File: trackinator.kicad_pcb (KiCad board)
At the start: 4 copper layers, 83 x 33.1 mm, 97 parts, among them J1 Conn_01x04_Pin, SW1 TS-1187A-B-A-B, SW2 TS-1187A-B-A-B, U1 M24C02-WMN, U2 ESP32-S3FH4R2, U3 LMZ21701SILR, U4 LMZ21701SILR, U5 SP3481EN, U6 FE2.1, U7 SP3481EN, U8 SP3481EN, Y1 12Mhz, Y2 40Mhz

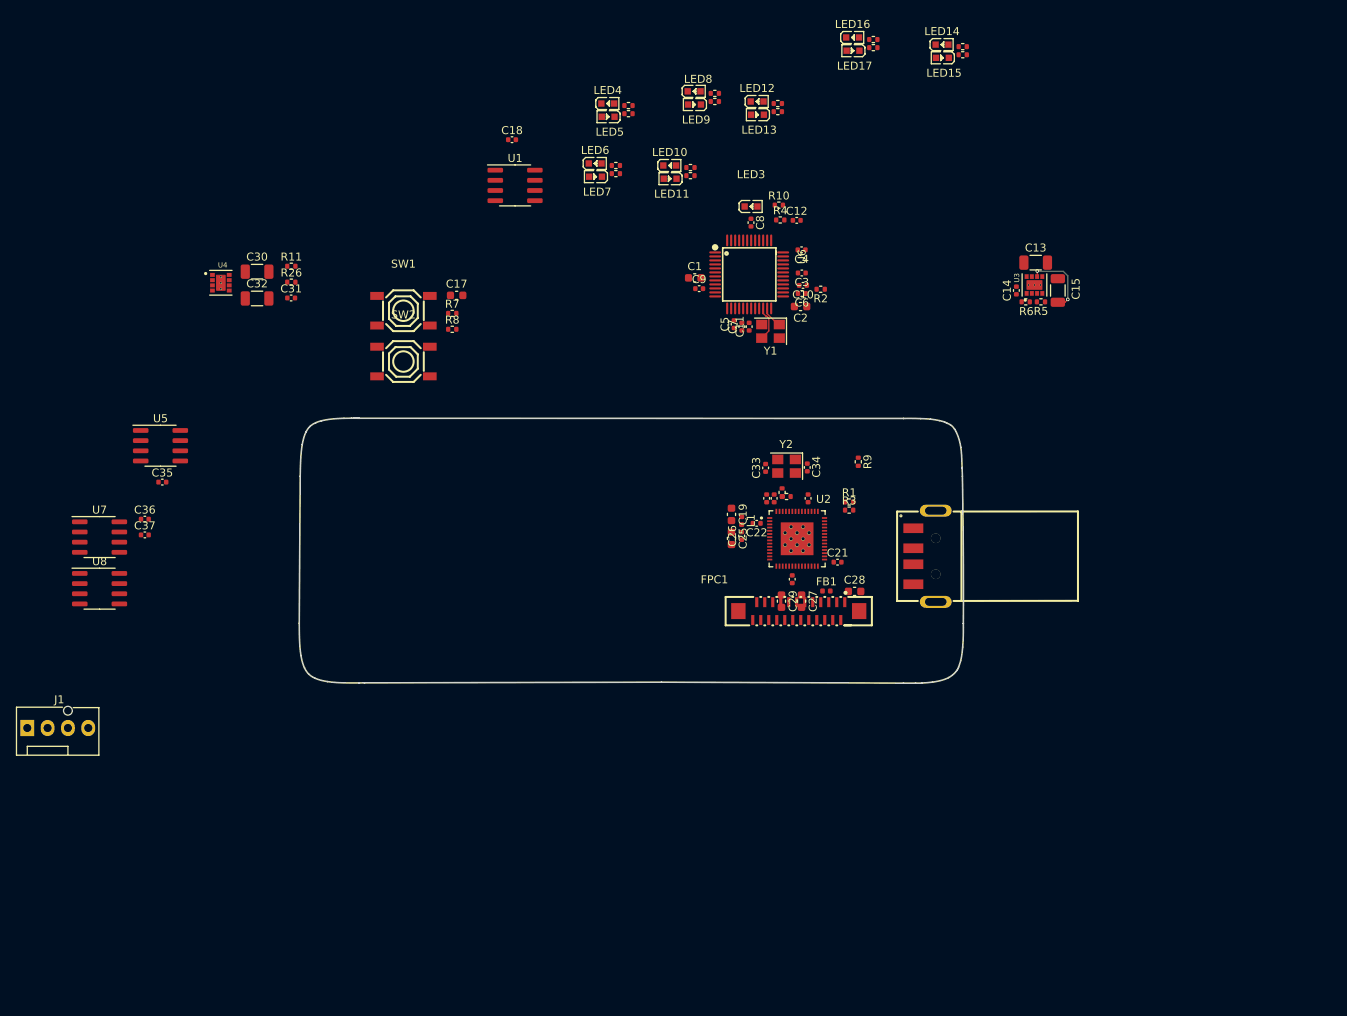
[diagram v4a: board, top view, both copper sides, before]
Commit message: more connectors and USB
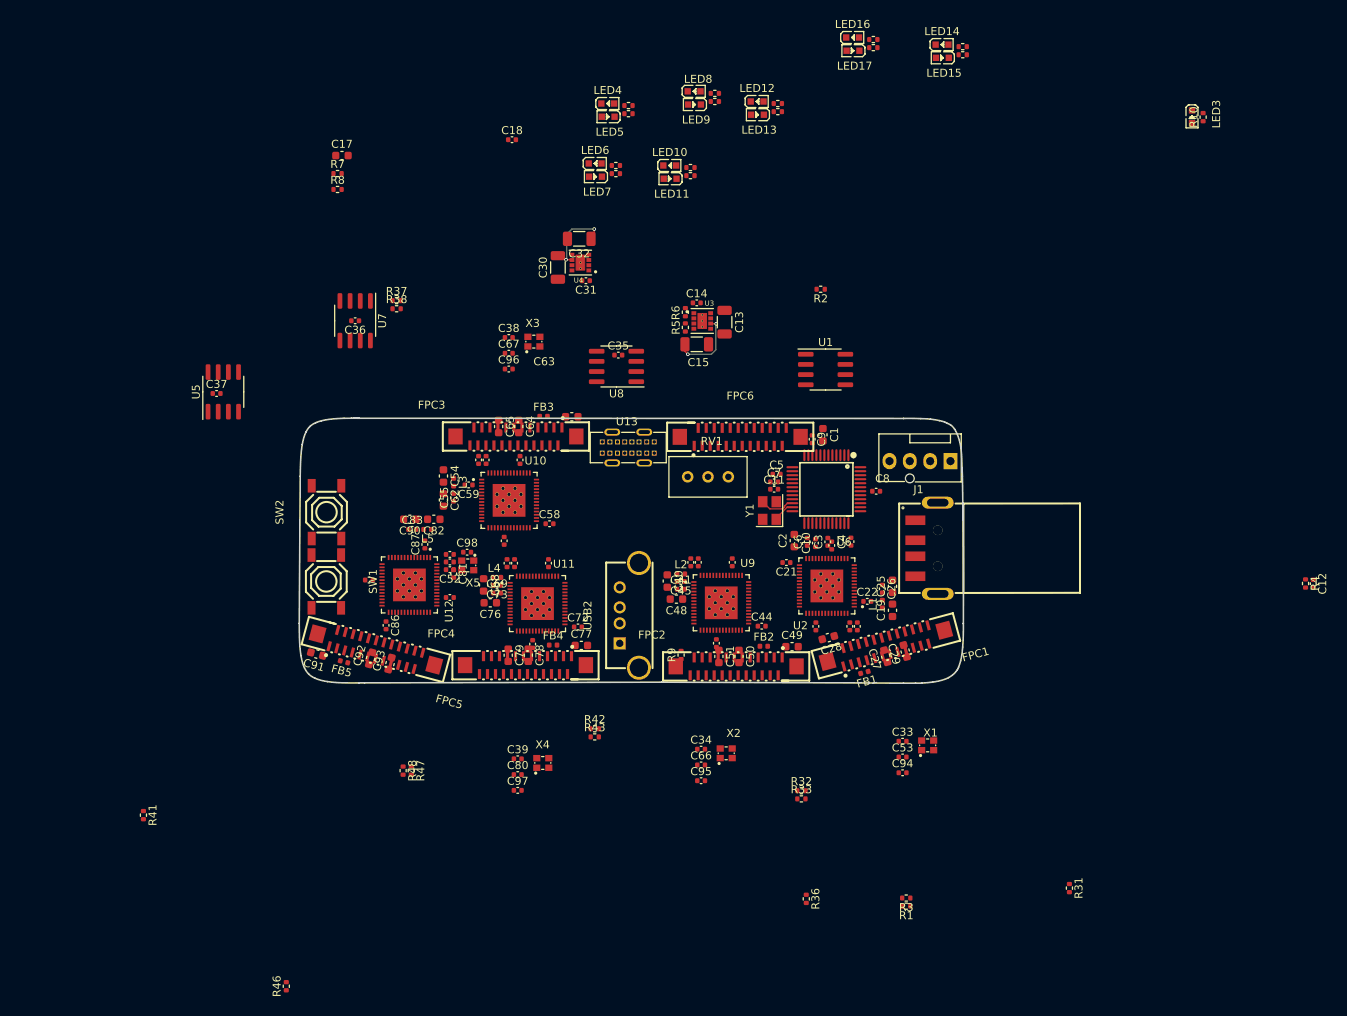
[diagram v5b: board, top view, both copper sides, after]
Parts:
- removed R11: 1M21, Resistor_SMD:R_0402_1005Metric
- removed R26: 383k, Resistor_SMD:R_0402_1005Metric
- removed R27, R28: 0, Resistor_SMD:R_0402_1005Metric
- removed Y2: 40Mhz, Crystal:Crystal_SMD_3225-4Pin_3.2x2.5mm
- added C38: 100p, Capacitor_SMD:C_0402_1005Metric, F.Cu at (169.0, 23.5)
- added C39: 100p, Capacitor_SMD:C_0402_1005Metric, F.Cu at (170.1, 76.1)
- added C40: 10u, Capacitor_SMD:C_0603_1608Metric, F.Cu at (188.8, 53.9)
- added C41: 100n, Capacitor_SMD:C_0402_1005Metric, F.Cu at (190.5, 54.9)
- added C42: 100n, Capacitor_SMD:C_0402_1005Metric, F.Cu at (192.7, 51.6)
- added C43: 100n, Capacitor_SMD:C_0402_1005Metric, F.Cu at (191.8, 51.6)
- added C44: 100n, Capacitor_SMD:C_0402_1005Metric, F.Cu at (200.6, 59.5)
- added C45: 100n, Capacitor_SMD:C_0402_1005Metric, F.Cu at (190.5, 53.9)
- added C46: 100n, Capacitor_SMD:C_0402_1005Metric, F.Cu at (196.9, 51.6)
- added C47: 100n, Capacitor_SMD:C_0402_1005Metric, F.Cu at (195.0, 61.7)
- added C48: 10u, Capacitor_SMD:C_0603_1608Metric, F.Cu at (190.0, 56.2)
- added C49: 10u, Capacitor_SMD:C_0603_1608Metric, F.Cu at (204.4, 62.1)
- added C50: 10u, Capacitor_SMD:C_0603_1608Metric, F.Cu at (197.8, 63.3)
- added C51: 10u, Capacitor_SMD:C_0603_1608Metric, F.Cu at (195.3, 63.3)
- added C52: 100p, Capacitor_SMD:C_0402_1005Metric, F.Cu at (161.6, 52.5)
- added C53: 100p, Capacitor_SMD:C_0402_1005Metric, F.Cu at (218.2, 75.9)
- added C54: 10u, Capacitor_SMD:C_0603_1608Metric, F.Cu at (160.8, 40.8)
- added C55: 100n, Capacitor_SMD:C_0402_1005Metric, F.Cu at (162.1, 43.5)
- added C56: 100n, Capacitor_SMD:C_0402_1005Metric, F.Cu at (166.2, 38.8)
- added C57: 100n, Capacitor_SMD:C_0402_1005Metric, F.Cu at (165.2, 38.8)
- added C58: 100n, Capacitor_SMD:C_0402_1005Metric, F.Cu at (174.1, 46.7)
- added C59: 100n, Capacitor_SMD:C_0402_1005Metric, F.Cu at (164.0, 41.9)
- added C60: 100n, Capacitor_SMD:C_0402_1005Metric, F.Cu at (170.4, 38.8)
- added C61: 100n, Capacitor_SMD:C_0402_1005Metric, F.Cu at (168.4, 48.9)
- added C62: 10u, Capacitor_SMD:C_0603_1608Metric, F.Cu at (160.8, 43.8)
- added C63: 10u, Capacitor_SMD:C_0603_1608Metric, F.Cu at (176.9, 33.4)
- added C64: 10u, Capacitor_SMD:C_0603_1608Metric, F.Cu at (170.3, 34.6)
- added C65: 10u, Capacitor_SMD:C_0603_1608Metric, F.Cu at (167.7, 34.6)
- added C66: 100p, Capacitor_SMD:C_0402_1005Metric, F.Cu at (193.1, 76.9)
- added C67: 100p, Capacitor_SMD:C_0402_1005Metric, F.Cu at (169.0, 25.4)
- added C68: 10u, Capacitor_SMD:C_0603_1608Metric, F.Cu at (165.9, 54.4)
- added C69: 100n, Capacitor_SMD:C_0402_1005Metric, F.Cu at (167.5, 55.4)
- added C70: 100n, Capacitor_SMD:C_0402_1005Metric, F.Cu at (169.7, 51.7)
- added C71: 100n, Capacitor_SMD:C_0402_1005Metric, F.Cu at (168.8, 51.7)
- added C72: 100n, Capacitor_SMD:C_0402_1005Metric, F.Cu at (177.7, 59.6)
- added C73: 100n, Capacitor_SMD:C_0402_1005Metric, F.Cu at (167.5, 54.4)
- added C74: 100n, Capacitor_SMD:C_0402_1005Metric, F.Cu at (174.0, 51.7)
- added C75: 100n, Capacitor_SMD:C_0402_1005Metric, F.Cu at (172.0, 61.8)
- added C76: 10u, Capacitor_SMD:C_0603_1608Metric, F.Cu at (166.7, 56.6)
- added C77: 10u, Capacitor_SMD:C_0603_1608Metric, F.Cu at (178.1, 62.0)
- added C78: 10u, Capacitor_SMD:C_0603_1608Metric, F.Cu at (171.4, 63.2)
- added C79: 10u, Capacitor_SMD:C_0603_1608Metric, F.Cu at (168.9, 63.2)
- added C80: 100p, Capacitor_SMD:C_0402_1005Metric, F.Cu at (170.1, 78.1)
- added C81: 100p, Capacitor_SMD:C_0402_1005Metric, F.Cu at (162.1, 53.0)
- added C82: 10u, Capacitor_SMD:C_0603_1608Metric, F.Cu at (159.6, 46.2)
- added C83: 100n, Capacitor_SMD:C_0402_1005Metric, F.Cu at (156.9, 47.4)
- added C84: 100n, Capacitor_SMD:C_0402_1005Metric, F.Cu at (161.6, 51.5)
- added C85: 100n, Capacitor_SMD:C_0402_1005Metric, F.Cu at (161.6, 50.6)
- added C86: 100n, Capacitor_SMD:C_0402_1005Metric, F.Cu at (153.7, 59.4)
- added C87: 100n, Capacitor_SMD:C_0402_1005Metric, F.Cu at (158.5, 49.3)
- added C88: 100n, Capacitor_SMD:C_0402_1005Metric, F.Cu at (161.6, 56.0)
- added C89: 100n, Capacitor_SMD:C_0402_1005Metric, F.Cu at (151.5, 53.8)
- added C90: 10u, Capacitor_SMD:C_0603_1608Metric, F.Cu at (156.6, 46.2)
- added C91: 10u, Capacitor_SMD:C_0603_1608Metric, F.Cu at (145.0, 63.0)
- added C92: 10u, Capacitor_SMD:C_0603_1608Metric, F.Cu at (151.7, 63.6)
- added C93: 10u, Capacitor_SMD:C_0603_1608Metric, F.Cu at (154.2, 64.2)
- added C94: 100n, Capacitor_SMD:C_0402_1005Metric, F.Cu at (218.2, 77.9)
- added C95: 100n, Capacitor_SMD:C_0402_1005Metric, F.Cu at (193.1, 78.9)
- added C96: 100n, Capacitor_SMD:C_0402_1005Metric, F.Cu at (169.0, 27.4)
- added C97: 100n, Capacitor_SMD:C_0402_1005Metric, F.Cu at (170.1, 80.1)
- added C98: 100n, Capacitor_SMD:C_0402_1005Metric, F.Cu at (163.8, 50.3)
- added FB2: 100R-800mA, Inductor_SMD:L_0402_1005Metric, F.Cu at (200.9, 62.1)
- added FB3: 100R-800mA, Inductor_SMD:L_0402_1005Metric, F.Cu at (173.4, 33.3)
- added FB4: 100R-800mA, Inductor_SMD:L_0402_1005Metric, F.Cu at (174.6, 61.9)
- added FB5: 100R-800mA, Inductor_SMD:L_0402_1005Metric, F.Cu at (148.4, 64.0)
- added FPC2: F0503-ZV-24-20T-R, easyeda2kicad:FPC-SMD_F0503-ZV-24-20T-R, F.Cu at (197.4, 64.6)
- added FPC3: F0503-ZV-24-20T-R, easyeda2kicad:FPC-SMD_F0503-ZV-24-20T-R, F.Cu at (169.9, 35.8)
- added FPC4: F0503-ZV-24-20T-R, easyeda2kicad:FPC-SMD_F0503-ZV-24-20T-R, F.Cu at (171.1, 64.4)
- added FPC5: F0503-ZV-24-20T-R, easyeda2kicad:FPC-SMD_F0503-ZV-24-20T-R, F.Cu at (152.4, 62.5)
- added FPC6: F0503-ZV-24-20T-R, easyeda2kicad:FPC-SMD_F0503-ZV-24-20T-R, F.Cu at (197.9, 35.9)
- added L2: 3n9, Inductor_SMD:L_0402_1005Metric, F.Cu at (190.5, 53.0)
- added L3: 3n9, Inductor_SMD:L_0402_1005Metric, F.Cu at (162.1, 41.6)
- added L4: 3n9, Inductor_SMD:L_0402_1005Metric, F.Cu at (167.5, 53.4)
- added L5: 3n9, Inductor_SMD:L_0402_1005Metric, F.Cu at (158.9, 47.4)
- added R31: 1k, Resistor_SMD:R_0402_1005Metric, F.Cu at (239.1, 92.3)
- added R32: 4k7, Resistor_SMD:R_0402_1005Metric, F.Cu at (205.6, 80.1)
- added R33: 4k7, Resistor_SMD:R_0402_1005Metric, F.Cu at (205.6, 81.1)
- added R36: 1k, Resistor_SMD:R_0402_1005Metric, F.Cu at (206.2, 93.6)
- added R37: 4k7, Resistor_SMD:R_0402_1005Metric, F.Cu at (155.0, 18.8)
- added R38: 4k7, Resistor_SMD:R_0402_1005Metric, F.Cu at (155.0, 19.9)
- added R41: 1k, Resistor_SMD:R_0402_1005Metric, F.Cu at (123.3, 83.2)
- added R42: 4k7, Resistor_SMD:R_0402_1005Metric, F.Cu at (179.8, 72.4)
- added R43: 4k7, Resistor_SMD:R_0402_1005Metric, F.Cu at (179.8, 73.4)
- added R46: 1k, Resistor_SMD:R_0402_1005Metric, F.Cu at (141.2, 104.5)
- added R47: 4k7, Resistor_SMD:R_0402_1005Metric, F.Cu at (156.8, 77.6)
- added R48: 4k7, Resistor_SMD:R_0402_1005Metric, F.Cu at (155.8, 77.6)
- added RV1: 50k, Potentiometer_THT:Potentiometer_Bourns_3296W_Vertical, F.Cu at (196.5, 40.9)
- added U10: ESP32-S3FH4R2, mylib:ESP32-S3FH4R2, F.Cu at (169.0, 43.8)
- added U11: ESP32-S3FH4R2, mylib:ESP32-S3FH4R2, F.Cu at (172.6, 56.7)
- added U12: ESP32-S3FH4R2, mylib:ESP32-S3FH4R2, F.Cu at (156.6, 54.4)
- added U13: TYPE-C 16PLC-H10.0, easyeda2kicad:TYPE-C-TH_16PLC-H10.0, F.Cu at (183.9, 37.2)
- added U9: ESP32-S3FH4R2, mylib:ESP32-S3FH4R2, F.Cu at (195.6, 56.6)
- added USB2: 1734366-1, easyeda2kicad:USB-A-TH_FUS264-FDSW3K, F.Cu at (184.1, 58.2)
- added X1: 40Mhz, easyeda2kicad:OSC-SMD_4P-L2.0-W1.6-BL_SIT1602BI, F.Cu at (221.4, 74.4)
- added X2: 40Mhz, easyeda2kicad:OSC-SMD_4P-L2.0-W1.6-BL_SIT1602BI, F.Cu at (196.2, 75.4)
- added X3: 40Mhz, easyeda2kicad:OSC-SMD_4P-L2.0-W1.6-BL_SIT1602BI, F.Cu at (172.1, 24.0)
- added X4: 40Mhz, easyeda2kicad:OSC-SMD_4P-L2.0-W1.6-BL_SIT1602BI, F.Cu at (173.3, 76.6)
- added X5: 40Mhz, easyeda2kicad:OSC-SMD_4P-L2.0-W1.6-BL_SIT1602BI, F.Cu at (163.9, 51.9)
- C33, C34: value 20p -> 100p
- moved J1 120.1 mm to (224.2, 38.9), turned to 180 degrees
- moved R4 79.8 mm to (268.6, 54.2), turned to -90 degrees
- moved C12 78.9 mm to (269.6, 54.2), turned to -90 degrees
- moved U8 70.3 mm to (182.5, 27.1), turned to 180 degrees
- moved C35 59.2 mm to (182.7, 25.7)
- moved LED3 56.3 mm to (254.4, -4.14), turned to -90 degrees
- moved R10 54.2 mm to (255.8, -4.09), turned to 90 degrees
- moved R1 51.0 mm to (218.7, 94.5), turned to 180 degrees
- moved R3 49.0 mm to (218.7, 93.5), turned to 180 degrees
- moved C15 45.6 mm to (192.5, 24.3), turned to 0 degrees
- moved U1 45.1 mm to (208.6, 27.5)
- moved U4 45.0 mm to (178.0, 14.1), turned to 180 degrees
- moved R5 44.6 mm to (191.1, 22.2), turned to 90 degrees
- moved R6 42.6 mm to (191.1, 20.3), turned to 90 degrees
- moved U7 41.9 mm to (149.8, 21.4), turned to -90 degrees
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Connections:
- C33 pad 2: Net-(C33-Pad2) -> Net-(U2-XTAL_P)
- C34 pad 1: Net-(U2-XTAL_N) -> Net-(X2-OUT)
- C34 pad 2: Net-(C33-Pad2) -> Net-(U9-XTAL_P)
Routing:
- net VDD_WS2812B: track 0.00 -> 9.08 mm, vias 0 -> 2

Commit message: savin' my work!
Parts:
- added C100: 10u, Capacitor_SMD:C_0603_1608Metric, F.Cu at (122.1, 54.7)
- added C101: 10u, Capacitor_SMD:C_0603_1608Metric, F.Cu at (120.2, 63.7)
- added C102: 10u, Capacitor_SMD:C_0603_1608Metric, F.Cu at (120.2, 66.7)
- added C99: 10u, Capacitor_SMD:C_0603_1608Metric, F.Cu at (122.1, 51.6)
- added R11: tbd, Resistor_SMD:R_0402_1005Metric, F.Cu at (124.1, 56.9)
- added R26: tbd, Resistor_SMD:R_0402_1005Metric, F.Cu at (126.0, 56.9)
- added R27: tbd, Resistor_SMD:R_0402_1005Metric, F.Cu at (122.1, 69.0)
- added R28: tbd, Resistor_SMD:R_0402_1005Metric, F.Cu at (124.1, 69.0)
- added U14: ADP125ARHZ-R7, easyeda2kicad:MSOP-8_L3.0-W3.0-P0.65-LS4.9-BL-EP, F.Cu at (124.5, 53.1)
- added U15: ADP125ARHZ-R7, easyeda2kicad:MSOP-8_L3.0-W3.0-P0.65-LS4.9-BL-EP, F.Cu at (122.7, 65.1)
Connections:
- U13 pad A1: unconnected-(U13-GND-PadA1) -> Net-(U13-GND-PadA1)
- U13 pad A10: unconnected-(U13-PadA10) -> Net-(U13-SHIELD-PadA10)
- U13 pad A12: unconnected-(U13-GND-PadA12) -> Net-(U13-GND-PadA1)
- U13 pad A2: unconnected-(U13-PadA2) -> Net-(U13-SHIELD-PadA10)
- U13 pad A4: unconnected-(U13-VBUS-PadA4) -> Net-(U13-VBUS-PadA4)
- U13 pad A9: unconnected-(U13-VBUS-PadA9) -> Net-(U13-VBUS-PadA4)
- U13 pad B1: unconnected-(U13-GND-PadB1) -> Net-(U13-GND-PadA1)
- U13 pad B10: unconnected-(U13-PadB10) -> Net-(U13-SHIELD-PadA10)
- U13 pad B12: unconnected-(U13-GND-PadB12) -> Net-(U13-GND-PadA1)
- U13 pad B2: unconnected-(U13-PadB2) -> Net-(U13-SHIELD-PadA10)
- U13 pad B4: unconnected-(U13-VBUS-PadB4) -> Net-(U13-VBUS-PadA4)
- U13 pad B9: unconnected-(U13-VBUS-PadB9) -> Net-(U13-VBUS-PadA4)
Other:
- board text added: "4 layer is a bit more expensive but has 2X the layers AND smaller traces and vias fill unused space on signal layers with power planes for distributed decoupling"
- board text removed: "4 layer is a bit more expensive but has 2X the layers AND smaller traces and vias"

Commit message: todo
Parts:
- renumbered U10 to Ue
